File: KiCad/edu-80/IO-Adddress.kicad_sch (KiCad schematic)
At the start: 7 parts, among them U14 PAL-002, U15 7400, U16 7400, U17 PAL-001, U18 CD4051, U19 CD4099, U20 CD4099

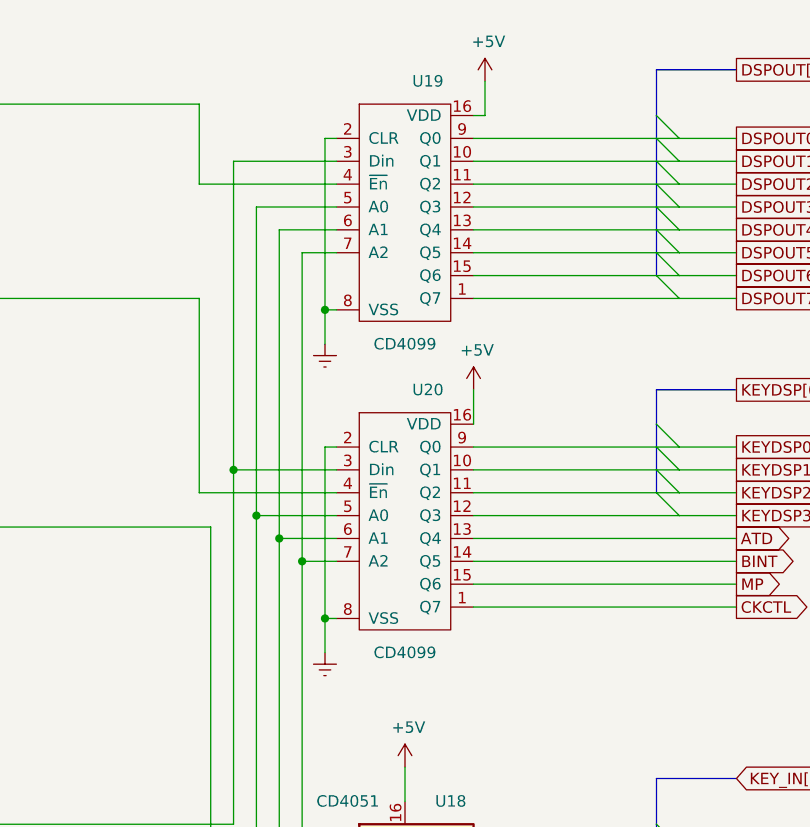
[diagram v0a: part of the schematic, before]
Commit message: Fixed lst of the errors, still two warnings
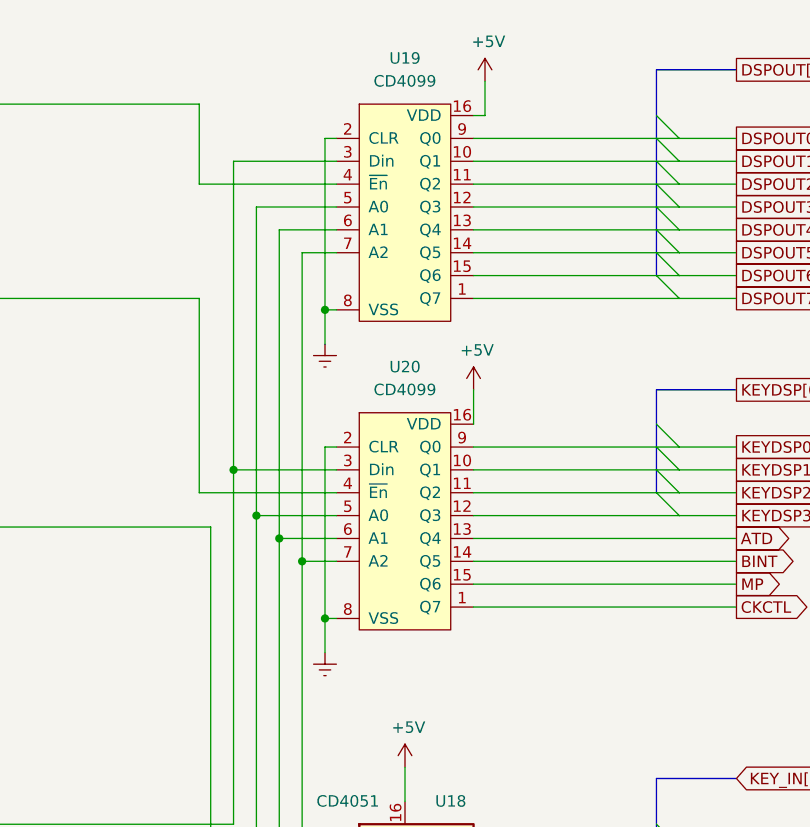
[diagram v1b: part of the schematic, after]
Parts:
- removed U19, U20: CD4099, symbol edu-80-rescue:CD4099-Edu-80_Symbol
- added U19, U20: CD4099, symbol Edu-80_Symbols:CD4099
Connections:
- net +5V: now also U19.16 (VDD), U20.16 (VDD)
- net A0: now also U19.5 (A0), U20.5 (A0)
- net A1: now also U19.6 (A1), U20.6 (A1)
- net A2: now also U19.7 (A2), U20.7 (A2)
- net ATD: now also U20.13 (Q4)
- net BINT: now also U20.14 (Q5)
- net CKCTL: now also U20.1 (Q7)
- net D0: now also U19.3 (Din), U20.3 (Din)
- net DSPOUT0: now also U19.9 (Q0)
- net DSPOUT1: now also U19.10 (Q1)
- net DSPOUT2: now also U19.11 (Q2)
- net DSPOUT3: now also U19.12 (Q3)
- net DSPOUT4: now also U19.13 (Q4)
- net DSPOUT5: now also U19.14 (Q5)
- net DSPOUT6: now also U19.15 (Q6)
- net DSPOUT7: now also U19.1 (Q7)
- net Earth: now also U19.2 (CLR), U19.8 (VSS), U20.2 (CLR), U20.8 (VSS)
- net KEYDSP0: now also U20.9 (Q0)
- net KEYDSP1: now also U20.10 (Q1)
- net KEYDSP2: now also U20.11 (Q2)
- net KEYDSP3: now also U20.12 (Q3)
- net MP: now also U20.15 (Q6)
- net at U16.10: now also U19.4 (~{En})
- net at U16.11: now also U20.4 (~{En})

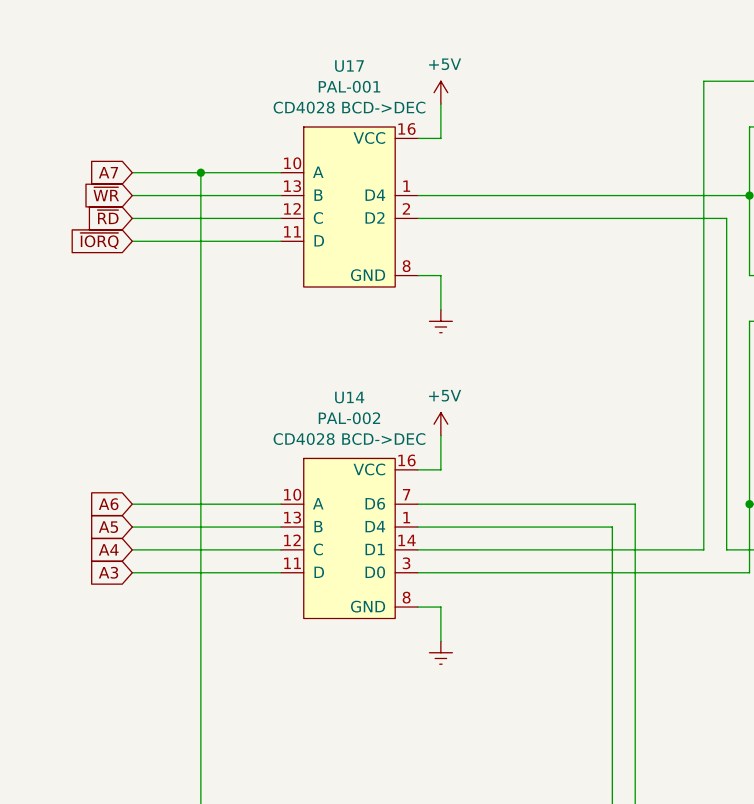
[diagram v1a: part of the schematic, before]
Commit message: Working on removing edu-80-rescue symbol library
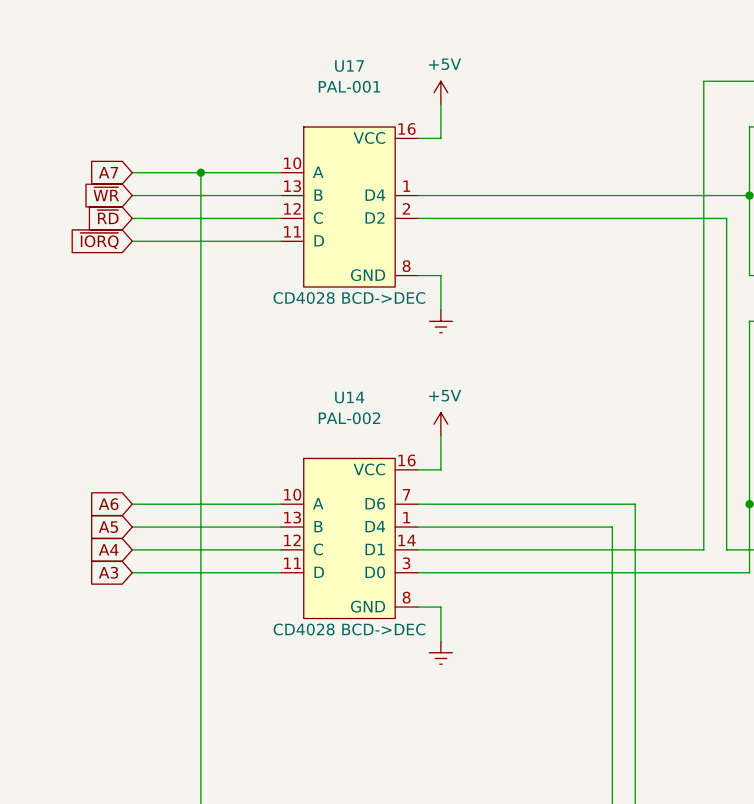
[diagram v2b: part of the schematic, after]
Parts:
- U14: symbol edu-80-rescue:PAL-002-Edu-80_Symbol -> Edu-80_Symbols:PAL-002
- U17: symbol edu-80-rescue:PAL-001-Edu-80_Symbol -> Edu-80_Symbols:PAL-001
- U18: symbol edu-80-rescue:CD4051-Edu-80_Symbol -> Edu-80_Symbols:CD4051
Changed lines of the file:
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@@
     )
   )
-  (symbol (lib_id "edu-80-rescue:CD4051-Edu-80_Symbol") (at 204.47 120.65 0) (unit 1)
+  (symbol (lib_id "Edu-80_Symbols:CD4051") (at 204.47 120.65 0) (unit 1)
     (in_bom yes) (on_board yes) (dnp no)
     (property "Reference" "U18" (at 209.55 107.95 0)
@@
     )
   )
-  (symbol (lib_id "edu-80-rescue:PAL-001-Edu-80_Symbol") (at 49.53 41.91 0) (unit 1)
+  (symbol (lib_id "Edu-80_Symbols:PAL-001") (at 49.53 41.91 0) (unit 1)
     (in_bom yes) (on_board yes) (dnp no)
     (property "Reference" "U17" (at 49.53 26.289 0)
@@
       (effects (font (size 1.27 1.27)) hide)
     )
-    (property "Replacement" "CD4028 BCD->DEC" (at 49.53 30.9118 0)
+    (property "Replacement" "CD4028 BCD->DEC" (at 49.53 52.07 0)
       (effects (font (size 1.27 1.27)))
     )
@@
     )
   )
-  (symbol (lib_id "edu-80-rescue:PAL-002-Edu-80_Symbol") (at 49.53 78.74 0) (unit 1)
+  (symbol (lib_id "Edu-80_Symbols:PAL-002") (at 49.53 78.74 0) (unit 1)
     (in_bom yes) (on_board yes) (dnp no)
     (property "Reference" "U14" (at 49.53 63.119 0)
@@
       (effects (font (size 1.27 1.27)) hide)
     )
-    (property "Replacement" "CD4028 BCD->DEC" (at 49.53 67.7418 0)
-      (effects (font (size 1.27 1.27)))
-    )
+    (property "Replacement" "CD4028 BCD->DEC" (at 49.53 88.9 0)
+      (effects (font (size 1.27 1.27)))
+    )

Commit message: Fixed the last of the EDR warnings/errors, adding footprints
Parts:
- U14, U17, U18, U19, U20: footprint (none) -> Package_DIP:DIP-16_W7.62mm
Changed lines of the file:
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@@
       (effects (font (size 1.27 1.27)) hide)
     )
-    (property "Datasheet" "http://www.ti.com/lit/gpn/sn7400" (at 104.14 30.48 0)
+    (property "Datasheet" "http://www.intersil.com/content/dam/Intersil/documents/cd40/cd4011bms-12bms-23bms.pdf" (at 104.14 30.48 0)
       (effects (font (size 1.27 1.27)) hide)
     )
@@
       (effects (font (size 1.27 1.27)) hide)
     )
-    (property "Datasheet" "http://www.ti.com/lit/gpn/sn7400" (at 104.14 52.07 0)
+    (property "Datasheet" "http://www.intersil.com/content/dam/Intersil/documents/cd40/cd4011bms-12bms-23bms.pdf" (at 104.14 52.07 0)
       (effects (font (size 1.27 1.27)) hide)
     )
@@
       (effects (font (size 1.27 1.27)) hide)
     )
-    (property "Datasheet" "http://www.ti.com/lit/gpn/sn7400" (at 104.14 77.47 0)
+    (property "Datasheet" "http://www.intersil.com/content/dam/Intersil/documents/cd40/cd4011bms-12bms-23bms.pdf" (at 104.14 77.47 0)
       (effects (font (size 1.27 1.27)) hide)
     )
@@
       (effects (font (size 1.27 1.27)))
     )
-    (property "Footprint" "" (at 204.47 130.81 0)
+    (property "Footprint" "Package_DIP:DIP-16_W7.62mm" (at 204.47 130.81 0)
       (effects (font (size 1.27 1.27)) hide)
     )
@@
       (effects (font (size 1.27 1.27)))
     )
-    (property "Footprint" "" (at 46.99 38.1 0)
+    (property "Footprint" "Package_DIP:DIP-16_W7.62mm" (at 46.99 38.1 0)
       (effects (font (size 1.27 1.27)) hide)
     )
@@
       (effects (font (size 1.27 1.27)))
     )
-    (property "Footprint" "" (at 46.99 74.93 0)
+    (property "Footprint" "Package_DIP:DIP-16_W7.62mm" (at 46.99 74.93 0)
       (effects (font (size 1.27 1.27)) hide)
     )
@@
       (effects (font (size 1.27 1.27)))
     )
-    (property "Footprint" "" (at 219.71 67.31 0)
+    (property "Footprint" "Package_DIP:DIP-16_W7.62mm" (at 219.71 67.31 0)
       (effects (font (size 1.27 1.27)) hide)
     )
@@
       (effects (font (size 1.27 1.27)))
     )
-    (property "Footprint" "" (at 219.71 33.02 0)
+    (property "Footprint" "Package_DIP:DIP-16_W7.62mm" (at 219.71 33.02 0)
       (effects (font (size 1.27 1.27)) hide)
     )
@@
       (effects (font (size 1.27 1.27)) hide)
     )
-    (property "Datasheet" "http://www.ti.com/lit/gpn/sn7400" (at 110.49 189.23 0)
-      (effects (font (size 1.27 1.27)) hide)
-    )
+    (property "Datasheet" "http://www.intersil.com/content/dam/Intersil/documents/cd40/cd4011bms-12bms-23bms.pdf" (at 110.49 189.23 0)
+      (effects (font (size 1.27 1.27)) hide)
+    )
